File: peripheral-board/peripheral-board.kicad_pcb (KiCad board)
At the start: 2 copper layers, 165 x 100 mm, 188 parts, among them CON1001 AVR-ISP-10, CON4001 BARREL_JACK, CON7001 SD_Card, IC1001 ATTINY48-A, J10001 DB15_FEMALE_HighDensity, J6001 FCR1295, P1001 Peripheral Bus, P1002 Power, P9001 VGA, SW1001 Power, SW2001 1, SW2002 2, SW2003 3, SW2004 4, SW2005 5, SW2006 6, SW2007 7, SW2008 8, SW2009 9, SW2010 0, SW2011 +, SW2012 ´, SW2013 BKSP, SW2014 TROLL, SW2015 §, SW2016 UP, SW2017 RMB, SW2018 Q, SW2019 W, SW2020 E, SW2021 R, SW2022 T, SW2023 Y, SW2024 U, SW2025 I, SW2026 O, SW2027 P, SW2028 Å, SW2029 ¨, SW2030 RETURN, SW2031 ALT_GR, SW2032 <, SW2033 LEFT, SW2034 MMB, SW2035 A, SW2036 S, SW2037 D, SW2038 F, SW2039 G, SW2040 H, SW2041 J, SW2042 K, SW2043 L, SW2044 Ö, SW2045 Ä, SW2046 ', SW2047 ESC, SW2048 TAB, SW2049 ALT, SW2050 DOWN, SW2051 LMB, SW2052 SHIFT_L, SW2053 Z, SW2054 X, SW2055 C, SW2056 V, SW2057 B, SW2058 N, SW2059 M, SW2060 ,, SW2061 ., SW2062 -, SW2063 SHIFT_R, SW2064 FN_R, SW2065 SPACE, SW2066 FN_L, SW2067 RIGHT, SW2068 CTRL, SW2069 SPACE, U2001 4017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

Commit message: audio circuitry
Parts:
- removed C7001: 1u, Capacitors_SMD:C_1206
- removed C7002, C7003: C_Small, Capacitors_SMD:C_0805
- removed CON7001: SD_Card, lib:TS-2198-01
- removed IC1001: ATTINY48-A, Housings_QFP:TQFP-32_7x7mm_Pitch0.8mm
- removed J6001: FCR1295, lib:FCR1295
- removed R7001, R7002: R, Resistors_SMD:R_0805
- removed RP2001: 10k, Resistors_SMD:R_Cat16-4
- removed U6001: TCA0372, Housings_SOIC:SOIC-16_7.5x10.3mm_Pitch1.27mm
- removed U6002, U6003: MCP4011, Housings_SOIC:SOIC-8_3.9x4.9mm_Pitch1.27mm
- added C7004: 100u, Capacitors_Tantalum_SMD:CP_Tantalum_Case-D_EIA-7343-31_Reflow, B.Cu at (316.5, 80.0)
- added C7005: 100n, Capacitors_SMD:C_0805, B.Cu at (349.7, 89.1)
- added C7006: 1u, Capacitors_SMD:C_0805, B.Cu at (357.8, 99.0)
- added C7007: 1u, Capacitors_SMD:C_0805, B.Cu at (370.2, 108.2)
- added C7008: 220u, Capacitors_Tantalum_SMD:CP_Tantalum_Case-D_EIA-7343-31_Reflow, B.Cu at (332.6, 92.8)
- added C7009: 1n, Capacitors_SMD:C_0805, B.Cu at (360.6, 89.1)
- added C7010: 47n, Capacitors_SMD:C_0805, B.Cu at (357.2, 82.7)
- added C7011: 100u, Capacitors_Tantalum_SMD:CP_Tantalum_Case-D_EIA-7343-31_Reflow, B.Cu at (347.7, 106.4)
- added C7012: 100n, Capacitors_SMD:C_0805, B.Cu at (362.6, 82.8)
- added C7013: 1u, Capacitors_SMD:C_0805, B.Cu at (371.5, 89.1)
- added C7014: 1u, Capacitors_SMD:C_0805, B.Cu at (368.1, 82.8)
- added C7015: 220u, Capacitors_Tantalum_SMD:CP_Tantalum_Case-D_EIA-7343-31_Reflow, B.Cu at (329.2, 80.0)
- added C7016: 1n, Capacitors_SMD:C_0805, B.Cu at (368.7, 95.5)
- added C7017: 47n, Capacitors_SMD:C_0805, B.Cu at (351.7, 82.7)
- added C8002: 1u, Capacitors_SMD:C_0805, B.Cu at (352.2, 150.9)
- added C8003: C_Small, Capacitors_SMD:C_0805, B.Cu at (346.1, 150.9)
- added C8004: C_Small, Capacitors_SMD:C_0805, B.Cu at (346.1, 144.6)
- added CON8001: SD_Card, lib:TS-2198-01, B.Cu at (131.0, 120.0)
- added J7001: FCR1295, lib:FCR1295, B.Cu at (339.5, 105.3)
- added LS7001: Speaker L, Socket_Strips:Socket_Strip_Straight_1x02_Pitch2.54mm, B.Cu at (317.3, 104.8)
- added LS7002: Speaker R, Socket_Strips:Socket_Strip_Straight_1x02_Pitch2.54mm, B.Cu at (317.3, 91.6)
- added R4001: 10k, Resistors_SMD:R_0805, B.Cu at (186.2, -0.95)
- added R4002: 330k, Resistors_SMD:R_0805, B.Cu at (191.7, 5.40)
- added R4003: 10k, Resistors_SMD:R_0805, B.Cu at (180.8, -7.30)
- added R4004: 10k, Resistors_SMD:R_0805, B.Cu at (186.2, 5.40)
- added R4005: 0R05, Resistors_SMD:R_0805, B.Cu at (175.3, -7.30)
- added R4006: 47k, Resistors_SMD:R_0805, B.Cu at (180.8, -0.95)
- added R4007: 626k, Resistors_SMD:R_0805, B.Cu at (175.3, -0.95)
- added R4008: 51k, Resistors_SMD:R_0805, B.Cu at (180.8, 5.40)
- added R4009: 412k, Resistors_SMD:R_0805, B.Cu at (169.9, -7.30)
- added R4010: R, Resistors_SMD:R_0805, B.Cu at (175.3, 5.40)
- added R4011: R, Resistors_SMD:R_0805, B.Cu at (191.7, -0.95)
- added R4012: 270k, Resistors_SMD:R_0805, B.Cu at (169.9, 5.40)
- added R4013: 13.3k, Resistors_SMD:R_0805, B.Cu at (169.9, -0.95)
- added R5001: 10k, Resistors_SMD:R_0805, B.Cu at (169.9, -17.6)
- added R5002: 150k, Resistors_SMD:R_0805, B.Cu at (169.9, -23.9)
- added R5003: 40R, Resistors_SMD:R_0805, B.Cu at (175.3, -17.6)
- added R5004: 40R, Resistors_SMD:R_0805, B.Cu at (180.8, -17.6)
- added R5005: 220k, Resistors_SMD:R_0805, B.Cu at (175.3, -23.9)
- added R5006: 10k, Resistors_SMD:R_0805, B.Cu at (180.8, -23.9)
- added R5007: 150k, Resistors_SMD:R_0805, B.Cu at (186.2, -17.6)
- added R5008: 40R, Resistors_SMD:R_0805, B.Cu at (191.7, -17.6)
- added R5009: 40R, Resistors_SMD:R_0805, B.Cu at (186.2, -23.9)
- added R5010: 220k, Resistors_SMD:R_0805, B.Cu at (191.7, -23.9)
- added R7003: 100k, Resistors_SMD:R_0805, B.Cu at (366.1, 89.1)
- added R7004: 10k, Resistors_SMD:R_0805, B.Cu at (364.8, 108.2)
- added R7005: 100k, Resistors_SMD:R_0805, B.Cu at (363.2, 95.5)
- added R7006: 10, Resistors_SMD:R_0805, B.Cu at (355.2, 89.1)
- added R7007: 100k, Resistors_SMD:R_0805, B.Cu at (364.8, 101.8)
- added R7008: 10k, Resistors_SMD:R_0805, B.Cu at (346.3, 82.7)
- added R7009: 10, Resistors_SMD:R_0805, B.Cu at (370.2, 101.8)
- added R8001: R, Resistors_SMD:R_0805, B.Cu at (345.5, 138.2)
- added R8002: R, Resistors_SMD:R_0805, B.Cu at (357.6, 150.9)
- added U1001: ATTINY48-A, Housings_QFP:TQFP-32_7x7mm_Pitch0.8mm, B.Cu at (99.8, 173.2)
- added U7001: LM386, Housings_SOIC:SOIC-8_3.9x4.9mm_Pitch1.27mm, B.Cu at (358.0, 106.8)
- added U7002: LM386, Housings_SOIC:SOIC-8_3.9x4.9mm_Pitch1.27mm, B.Cu at (343.0, 93.2)
- added U7003: MCP4011, Housings_SOIC:SOIC-8_3.9x4.9mm_Pitch1.27mm, B.Cu at (351.0, 96.8)
- added U7004: MCP4011, Housings_SOIC:SOIC-8_3.9x4.9mm_Pitch1.27mm, B.Cu at (339.5, 83.2)

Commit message: power supply component placement
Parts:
- removed CONN8001: 10056847-XY1LF, lib:10056847-XY1LF
- removed P9001: VGA, Socket_Strips:Socket_Strip_Straight_1x06
- removed R4010, R4011: R, Resistors_SMD:R_0805
- added C7001: 100n, Capacitors_SMD:C_0805, B.Cu at (261.9, 144.4)
- added C7002: 100n, Capacitors_SMD:C_0805, B.Cu at (256.4, 144.4)
- added CONN9001: 10056847-XY1LF, lib:10056847-XY1LF, B.Cu at (241.9, 86.3)
- added Q4001: IRLML2244TRPbF, TO_SOT_Packages_SMD:SOT-23, B.Cu at (217.6, 63.3)
- added Q5001: IRLML2244TRPbF, TO_SOT_Packages_SMD:SOT-23, B.Cu at (201.0, -16.0)
- added Q5002: IRLML2244TRPbF, TO_SOT_Packages_SMD:SOT-23, B.Cu at (209.5, -15.0)
- added R1003: R, Resistors_SMD:R_0805, B.Cu at (60.8, 122.4)
- added R1004: R, Resistors_SMD:R_0805, B.Cu at (59.1, 115.6)
- added R1005: R, Resistors_SMD:R_0805, B.Cu at (116.0, 162.0)
- added R9001: 47k, Resistors_SMD:R_0805, F.Cu at (101.8, 153.6)
- added RP2001: 10k, Resistors_SMD:R_Cat16-4, F.Cu at (134.6, 131.0)
- C8003, C8004: value C_Small -> 100n
- R8001, R8002: value R -> 47k
- moved C8003 261.3 mm to (87.9, 191.0)
- moved C8004 261.3 mm to (87.9, 184.7)
- moved R8001 261.3 mm to (87.3, 178.3)
- moved C8002 261.3 mm to (94.0, 191.0)
- moved R8002 261.3 mm to (99.4, 191.0)
- moved J7001 95.4 mm to (250.0, 72.2)
- moved C7008 92.2 mm to (240.5, 97.5), turned to 90 degrees
- moved LS7001 89.0 mm to (238.0, 64.5), turned to 270 degrees
- moved R4009 86.3 mm to (224.6, 59.5), turned to 180 degrees
- moved C7015 84.5 mm to (246.5, 97.5), turned to 90 degrees
- moved C7016 82.8 mm to (293.0, 129.1)
- moved R7008 82.8 mm to (270.6, 116.3)
- moved R7006 82.8 mm to (279.5, 122.7)
- moved C7005 82.8 mm to (274.0, 122.7)
- moved C7006 82.8 mm to (282.1, 132.6)
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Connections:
- net CLK12 renamed /CLK12
- net CLK33 renamed /CLK33
- C7004 pad 1: +BATT -> VAA
- C7005 pad 1: +BATT -> VAA
- C7007 pad 2: /Audio/L -> /AUDIO_L
- C7011 pad 1: +BATT -> VAA
- C7012 pad 1: +BATT -> VAA
- C7014 pad 2: /Audio/R -> /AUDIO_R
- CON8001 pad 1: /SD Card/SS -> /SPI_SS3
- CON8001 pad 2: /SD Card/MOSI -> /SPI_MOSI
- CON8001 pad 5: /SD Card/SCK -> /SPI_SCK
- CON8001 pad 7: /SD Card/MISO -> /SPI_MISO
- D2001 pad 1: /Keyboard/Q0 -> /KBD_Q0
- D2002 pad 1: /Keyboard/Q0 -> /KBD_Q0
- D2003 pad 1: /Keyboard/Q0 -> /KBD_Q0
- D2004 pad 1: /Keyboard/Q0 -> /KBD_Q0
- D2005 pad 1: /Keyboard/Q0 -> /KBD_Q0
- D2006 pad 1: /Keyboard/Q0 -> /KBD_Q0
- D2007 pad 1: /Keyboard/Q0 -> /KBD_Q0
- D2008 pad 1: /Keyboard/Q0 -> /KBD_Q0
- D2009 pad 1: /Keyboard/Q0 -> /KBD_Q0
- D2010 pad 1: /Keyboard/Q0 -> /KBD_Q0
- D2011 pad 1: /Keyboard/Q0 -> /KBD_Q0
- D2012 pad 1: /Keyboard/Q0 -> /KBD_Q0
- D2013 pad 1: /Keyboard/Q0 -> /KBD_Q0
- D2014 pad 1: /Keyboard/Q0 -> /KBD_Q0
- D2015 pad 1: /Keyboard/Q2 -> /KBD_Q2
- D2016 pad 1: /Keyboard/Q0 -> /KBD_Q0
- D2017 pad 1: /Keyboard/Q3 -> /KBD_Q3
- D2018 pad 1: /Keyboard/Q1 -> /KBD_Q1
- D2019 pad 1: /Keyboard/Q1 -> /KBD_Q1
- D2020 pad 1: /Keyboard/Q1 -> /KBD_Q1
- D2021 pad 1: /Keyboard/Q1 -> /KBD_Q1
- D2022 pad 1: /Keyboard/Q1 -> /KBD_Q1
- D2023 pad 1: /Keyboard/Q1 -> /KBD_Q1
- D2024 pad 1: /Keyboard/Q1 -> /KBD_Q1
- D2025 pad 1: /Keyboard/Q1 -> /KBD_Q1
- D2026 pad 1: /Keyboard/Q1 -> /KBD_Q1
- D2027 pad 1: /Keyboard/Q1 -> /KBD_Q1
- D2028 pad 1: /Keyboard/Q1 -> /KBD_Q1
- D2029 pad 1: /Keyboard/Q1 -> /KBD_Q1
- D2030 pad 1: /Keyboard/Q1 -> /KBD_Q1
- D2031 pad 1: /Keyboard/Q1 -> /KBD_Q1
- D2032 pad 1: /Keyboard/Q1 -> /KBD_Q1
- D2033 pad 1: /Keyboard/Q3 -> /KBD_Q3
- D2034 pad 1: /Keyboard/Q2 -> /KBD_Q2
- D2035 pad 1: /Keyboard/Q2 -> /KBD_Q2
- D2036 pad 1: /Keyboard/Q2 -> /KBD_Q2
- D2037 pad 1: /Keyboard/Q2 -> /KBD_Q2
- D2038 pad 1: /Keyboard/Q2 -> /KBD_Q2
- D2039 pad 1: /Keyboard/Q2 -> /KBD_Q2
- D2040 pad 1: /Keyboard/Q2 -> /KBD_Q2
- D2041 pad 1: /Keyboard/Q2 -> /KBD_Q2
- D2042 pad 1: /Keyboard/Q2 -> /KBD_Q2
- D2043 pad 1: /Keyboard/Q2 -> /KBD_Q2
- D2044 pad 1: /Keyboard/Q2 -> /KBD_Q2
- D2045 pad 1: /Keyboard/Q2 -> /KBD_Q2
- D2046 pad 1: /Keyboard/Q2 -> /KBD_Q2
- D2047 pad 1: /Keyboard/Q2 -> /KBD_Q2
- D2048 pad 1: /Keyboard/Q2 -> /KBD_Q2
- D2049 pad 1: /Keyboard/Q0 -> /KBD_Q0
- D2050 pad 1: /Keyboard/Q2 -> /KBD_Q2
- D2051 pad 1: /Keyboard/Q1 -> /KBD_Q1
- D2052 pad 1: /Keyboard/Q3 -> /KBD_Q3
- D2053 pad 1: /Keyboard/Q3 -> /KBD_Q3
- D2054 pad 1: /Keyboard/Q3 -> /KBD_Q3
- D2055 pad 1: /Keyboard/Q3 -> /KBD_Q3
- D2056 pad 1: /Keyboard/Q3 -> /KBD_Q3
- D2057 pad 1: /Keyboard/Q1 -> /KBD_Q1
- D2058 pad 1: /Keyboard/Q0 -> /KBD_Q0
- D2059 pad 1: /Keyboard/Q3 -> /KBD_Q3
- D2060 pad 1: /Keyboard/Q3 -> /KBD_Q3
- D2061 pad 1: /Keyboard/Q3 -> /KBD_Q3
- D2062 pad 1: /Keyboard/Q3 -> /KBD_Q3
- D2063 pad 1: /Keyboard/Q3 -> /KBD_Q3
- D2064 pad 1: /Keyboard/Q3 -> /KBD_Q3
- D2065 pad 1: /Keyboard/Q3 -> /KBD_Q3
- D2066 pad 1: /Keyboard/Q3 -> /KBD_Q3
- D2067 pad 1: /Keyboard/Q3 -> /KBD_Q3
- D2068 pad 1: /Keyboard/Q3 -> /KBD_Q3
- D4001 pad 1: +3V3 -> VAA
- J7001 pad 1: /Audio/DETECT -> /AUD_DET
- R1001 pad 1: Net-(R1001-Pad1) -> /I2C_SCL
- R1001 pad 2: Net-(R1001-Pad2) -> +3V3
- R1002 pad 1: Net-(R1002-Pad1) -> /I2C_SDA
- R1002 pad 2: Net-(R1002-Pad2) -> +3V3
- R7005 pad 2: /Audio/DETECT -> /AUD_DET
- SW1001 pad 2: Net-(SW1001-Pad2) -> /PWR_BTN
- U1001 pad 1: Net-(U1001-Pad1) -> /EXTINT0
- U1001 pad 10: Net-(U1001-Pad10) -> /KBD_Q2
- U1001 pad 11: Net-(U1001-Pad11) -> /KBD_Q3
- U1001 pad 12: Net-(U1001-Pad12) -> /PWR_SHDN_3
- U1001 pad 13: Net-(U1001-Pad13) -> /PWR_SHDN_24
- U1001 pad 14: /SPI_SS -> /SPI_SS2
- U1001 pad 19: Net-(U1001-Pad19) -> /EXT_DET
- U1001 pad 2: Net-(U1001-Pad2) -> /KBD_Q0
- U1001 pad 20: Net-(U1001-Pad20) -> /PWR_BTN
- U1001 pad 22: Net-(U1001-Pad22) -> /EXT_AN
- U1001 pad 25: Net-(U1001-Pad25) -> /PWRON_RESET
- U1001 pad 26: Net-(U1001-Pad26) -> /CPURST
- U1001 pad 29: Net-(U1001-Pad29) -> /RESET
- U1001 pad 3: Net-(U1001-Pad3) -> /KBD_CLK
- U1001 pad 30: Net-(U1001-Pad30) -> /AUD_UD
- U1001 pad 31: Net-(U1001-Pad31) -> /AUD_CS_L
- U1001 pad 32: Net-(U1001-Pad32) -> /AUD_CS_R
- U1001 pad 6: Net-(U1001-Pad6) -> /KBD_RST
- U1001 pad 7: Net-(U1001-Pad7) -> /AUD_DET
- U1001 pad 9: Net-(U1001-Pad9) -> /KBD_Q1
- U2002 pad 14: /Keyboard/CLK -> /KBD_CLK
- U2003 pad 2: /Keyboard/~RESET -> /KBD_RST
- U2003 pad 4: /Keyboard/CLK -> /KBD_CLK
- U3001 pad 1: /Mouse/X -> /MOUSE_X
- U3001 pad 3: /Mouse/Y -> /MOUSE_Y
- U4001 pad 1: +3V3 -> VAA
- U4001 pad 4: /Power Supply/SHDN -> /PWR_SHDN_3
- U4002 pad 4: Net-(Q4002-Pad1) -> /PWR_SHDN_24
- U4002 pad 5: +3V3 -> VAA
- U5001 pad 5: /RTC/SDA -> /I2C_SCL
- U5001 pad 6: /RTC/SCL -> /I2C_SDA
- U7001 pad 6: +BATT -> VAA
- U7002 pad 6: +BATT -> VAA
- U7003 pad 5: /Audio/~CS_L -> /AUD_CS_L
- U7003 pad 8: /Audio/UP/~DOWN -> /AUD_UD
- U7004 pad 5: /Audio/~CS_R -> /AUD_CS_R
- U7004 pad 8: /Audio/UP/~DOWN -> /AUD_UD
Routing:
- net /Keyboard/Q1: track 464.3 -> 0.00 mm
- net /KBD_Q1: track 0.00 -> 464.3 mm
- net /Keyboard/Q2: track 409.5 -> 0.00 mm
- net /KBD_Q2: track 0.00 -> 409.5 mm
- net /Keyboard/Q0: track 372.0 -> 0.00 mm
- net /KBD_Q0: track 0.00 -> 372.0 mm
- net /Keyboard/Q3: track 297.0 -> 0.00 mm
- net /KBD_Q3: track 0.00 -> 297.0 mm
- net /Keyboard/CLK: track 12.3 -> 0.00 mm
- net /KBD_CLK: track 0.00 -> 12.3 mm

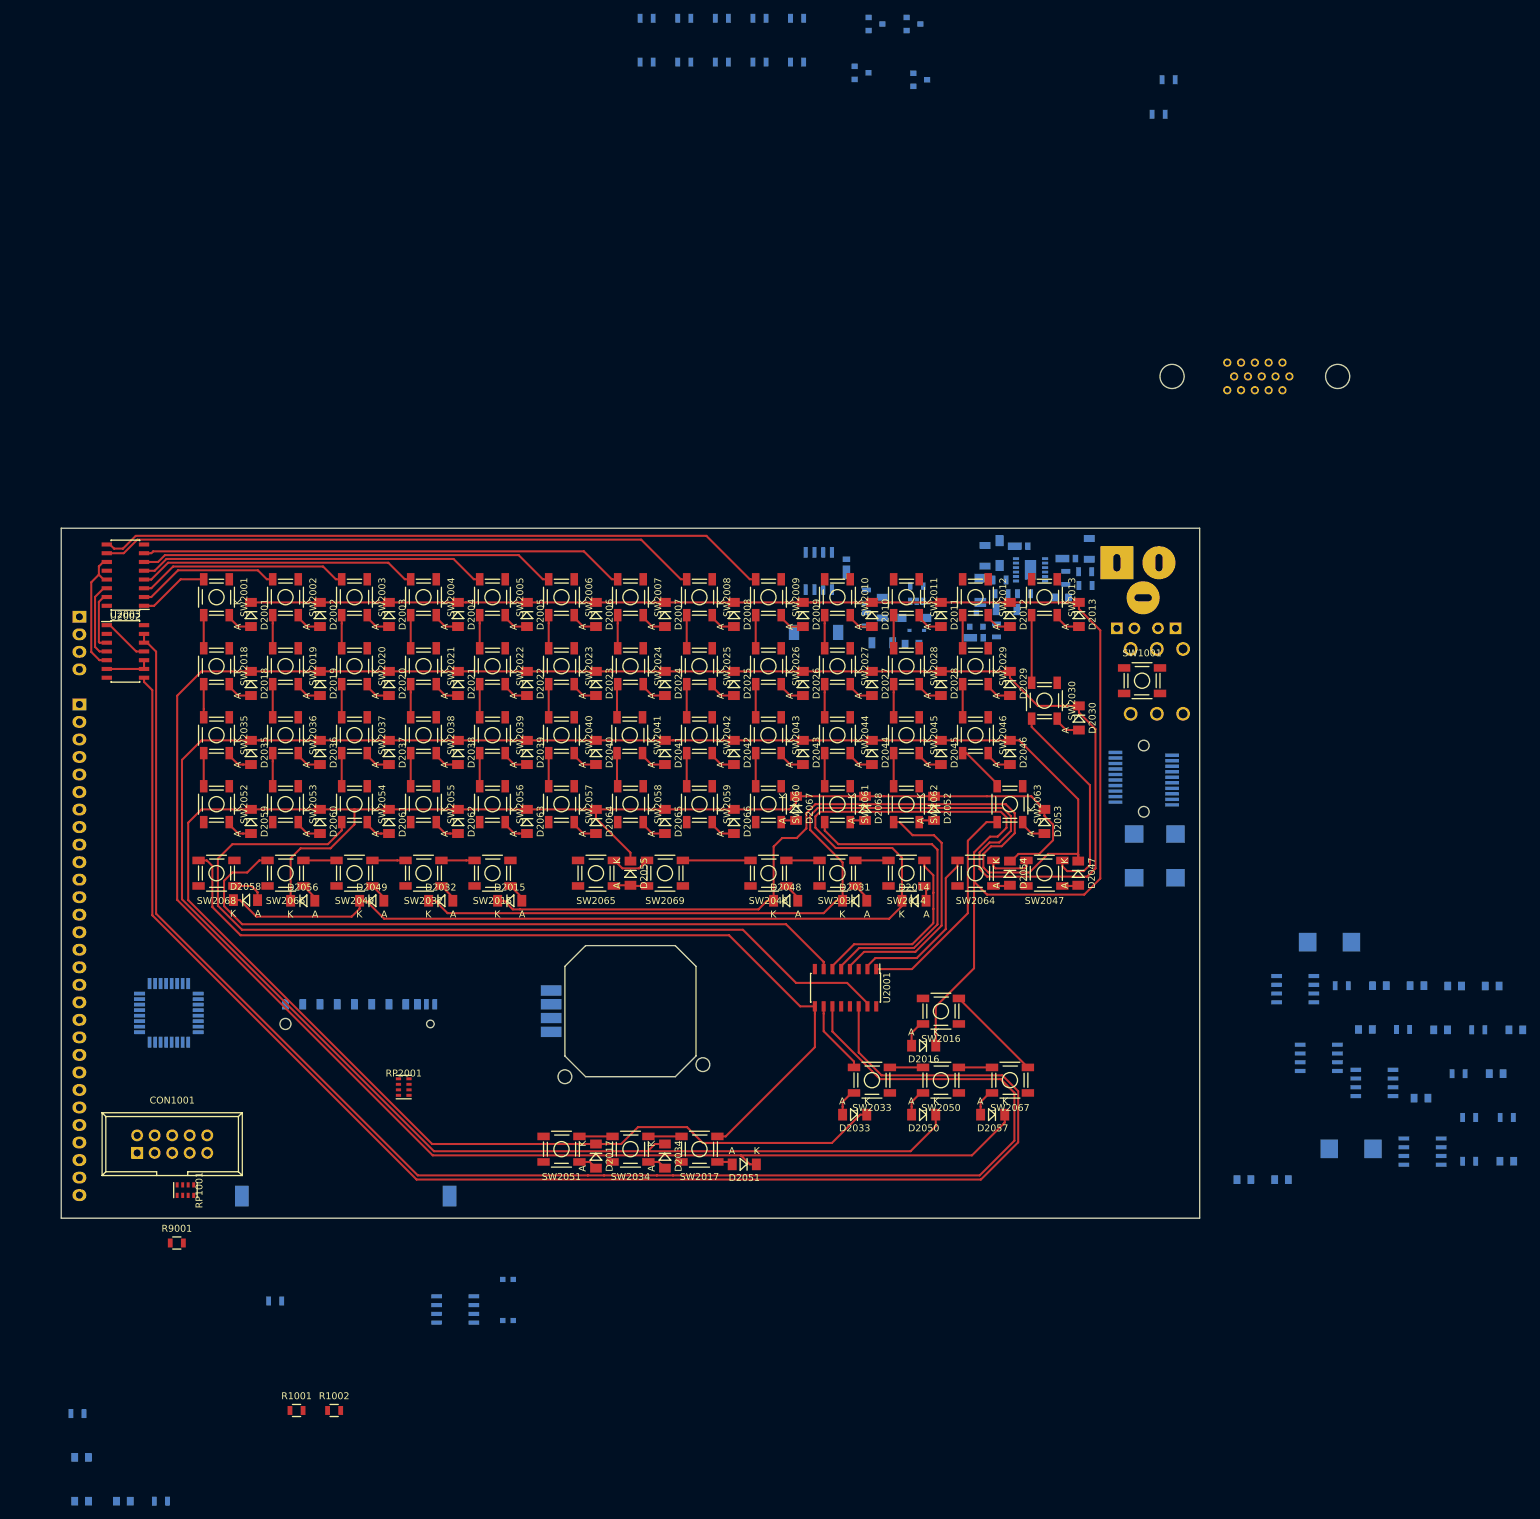
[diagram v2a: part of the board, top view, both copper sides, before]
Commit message: audio components placement
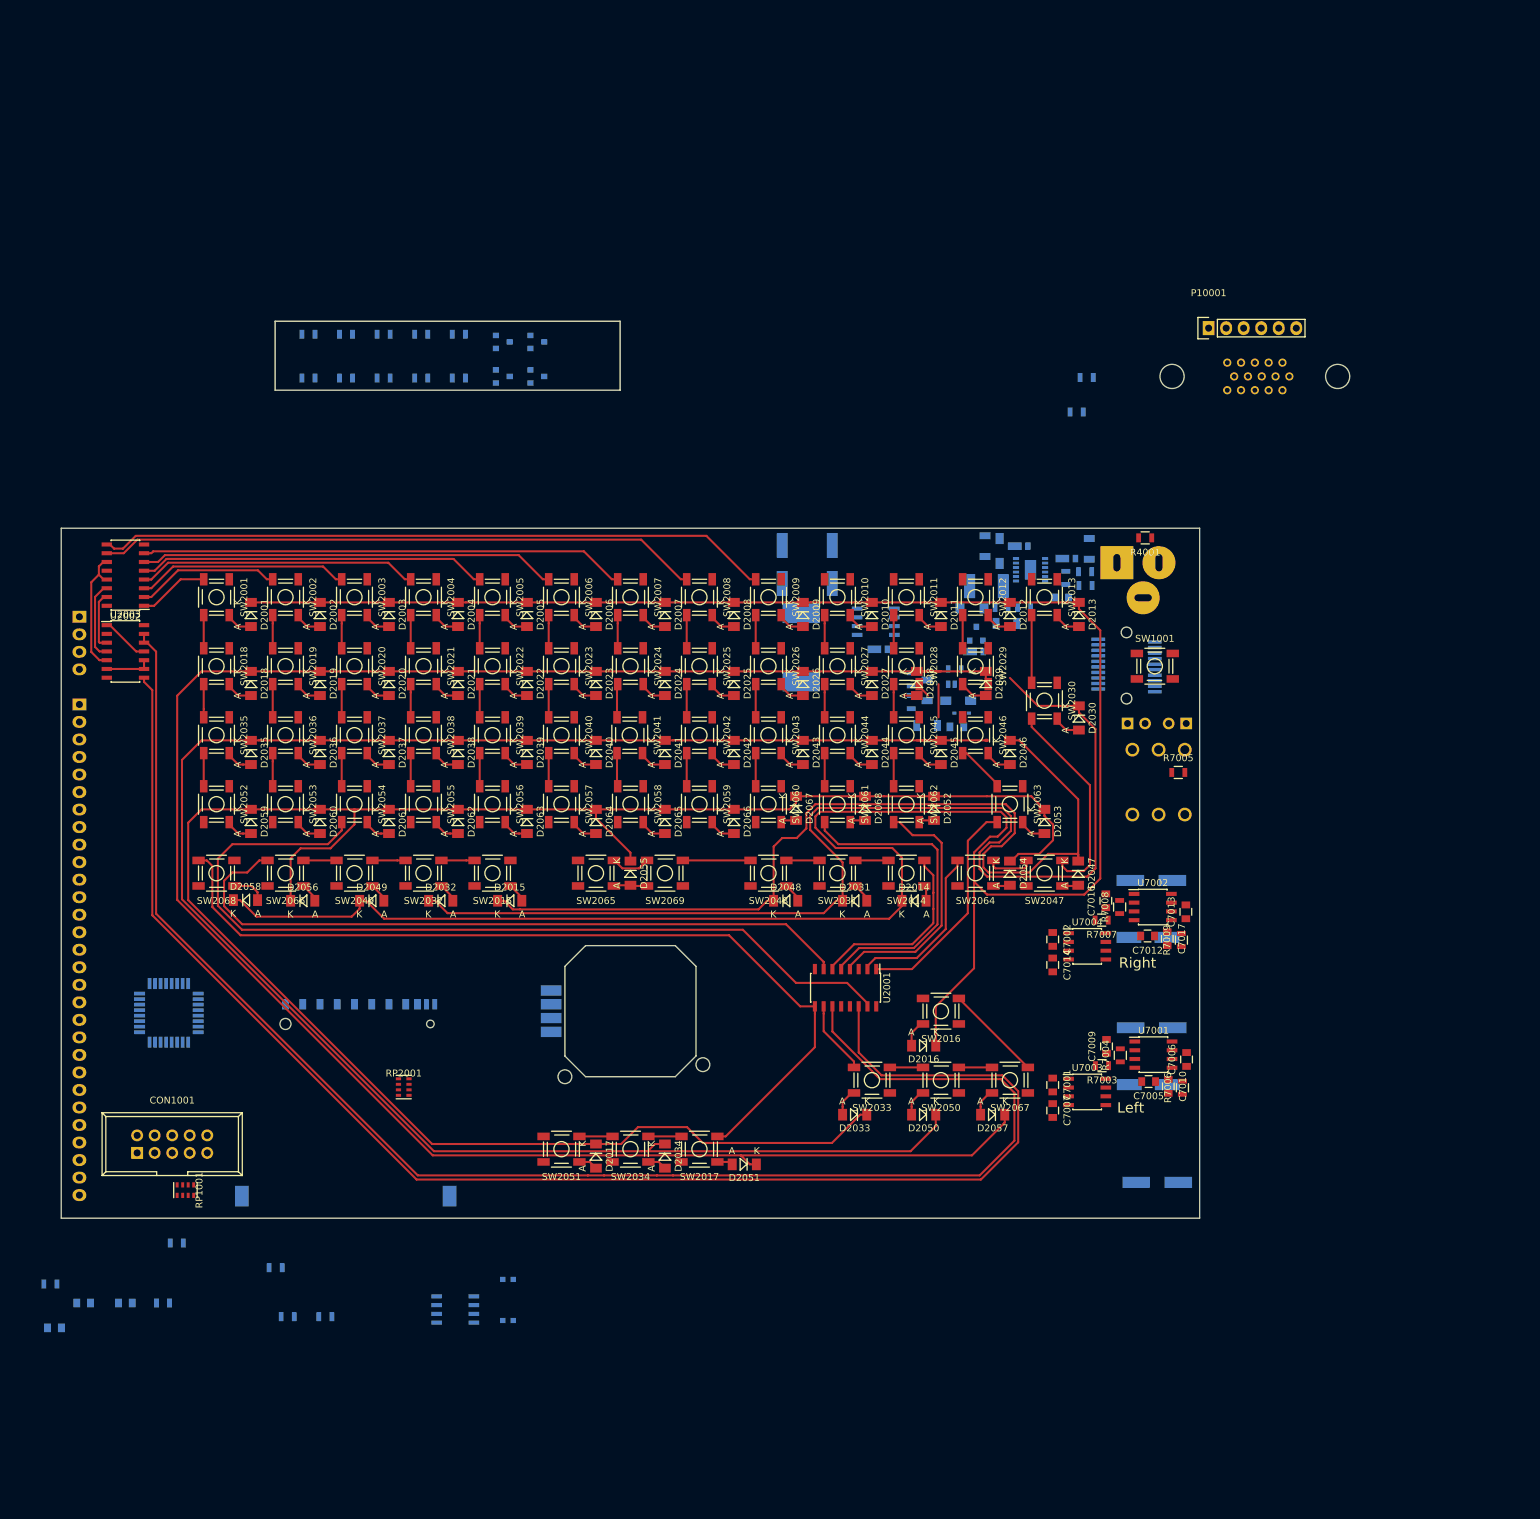
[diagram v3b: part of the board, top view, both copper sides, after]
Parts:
- added C4010: 100u, Capacitors_SMD:c_elec_6.3x5.8, B.Cu at (189.5, 55.3)
- added C4011: 100u, Capacitors_SMD:c_elec_6.3x5.8, B.Cu at (196.8, 55.3)
- added C7003: 10u, Capacitors_SMD:c_elec_6.3x5.8, B.Cu at (242.5, 109.3)
- added P10001: VGA, Socket_Strips:Socket_Strip_Straight_1x06, F.Cu at (251.3, 21.0)
- C7001, C7002, C7005, C7006, C7007, C7009, C7010, C7012, C7013, C7014, C7016, C7017, R4001, R7003, R7004, R7005, R7006, R7007, R7008, R7009, U7001, U7002, U7003, U7004: moved to F.Cu
- C7004: value 100u -> 220u; footprint Capacitors_Tantalum_SMD:CP_Tantalum_Case-D_EIA-7343-31_Reflow -> Capacitors_SMD:c_elec_8x6.7
- C7008, C7015: footprint Capacitors_Tantalum_SMD:CP_Tantalum_Case-D_EIA-7343-31_Reflow -> Capacitors_SMD:c_elec_8x6.7
- C7011: value 100u -> 10u; footprint Capacitors_Tantalum_SMD:CP_Tantalum_Case-D_EIA-7343-31_Reflow -> Capacitors_SMD:c_elec_6.3x5.8
- L4003: footprint Choke_SMD:Choke_SMD_7.3x7.3_H4.5 -> Choke_SMD:Choke_SMD_12x12mm_h6mm
- R1001, R1002, R9001: moved to B.Cu
- R4005: footprint Resistors_SMD:R_0805 -> Resistors_SMD:R_1812
- moved U5003 75.3 mm to (149.0, 23.0)
- moved Q5002 70.2 mm to (154.0, 28.0)
- moved Q5001 68.1 mm to (149.0, 28.0)
- moved U5002 67.3 mm to (154.0, 23.0)
- moved R5001 67.1 mm to (120.8, 28.2)
- moved R5002 67.1 mm to (120.8, 21.9)
- moved R5003 67.1 mm to (126.3, 28.2)
- moved R5005 67.1 mm to (126.3, 21.9)
- moved R5007 67.1 mm to (137.2, 28.2)
- moved R5008 67.1 mm to (142.6, 28.2)
- moved R5009 67.1 mm to (137.2, 21.9)
- moved R5010 67.1 mm to (142.6, 21.9)
- moved R5004 67.1 mm to (131.7, 28.2)
- moved R5006 67.1 mm to (131.7, 21.9)
- moved C7007 66.2 mm to (228.7, 134.4), turned to 270 degrees
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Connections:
- net /SD Card/WP renamed /SD_WP
- CON8001 pad 10: /SD Card/DETECT -> /SD_DET
- R8002 pad 2: /SD Card/DETECT -> /SD_DET
- U1001 pad 8: Net-(U1001-Pad8) -> /SD_DET
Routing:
- net (no net): track 0.00 -> 15.0 mm
- net /KBD_Q2: track 409.5 -> 399.3 mm
- net /Keyboard/COL11: track 49.3 -> 46.7 mm
- net Net-(D2029-Pad2): track 4.04 -> 1.85 mm
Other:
- board size 165 x 100 mm -> 165 x 130 mm
- board text added: "Left"
- board text added: "Right"
- board text removed: "SMPS"
